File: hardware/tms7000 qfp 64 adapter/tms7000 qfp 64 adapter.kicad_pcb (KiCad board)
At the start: 2 copper layers, 45.1 x 52.1 mm, 4 parts, among them J1 qfp 64, U1 DIP40 male pins

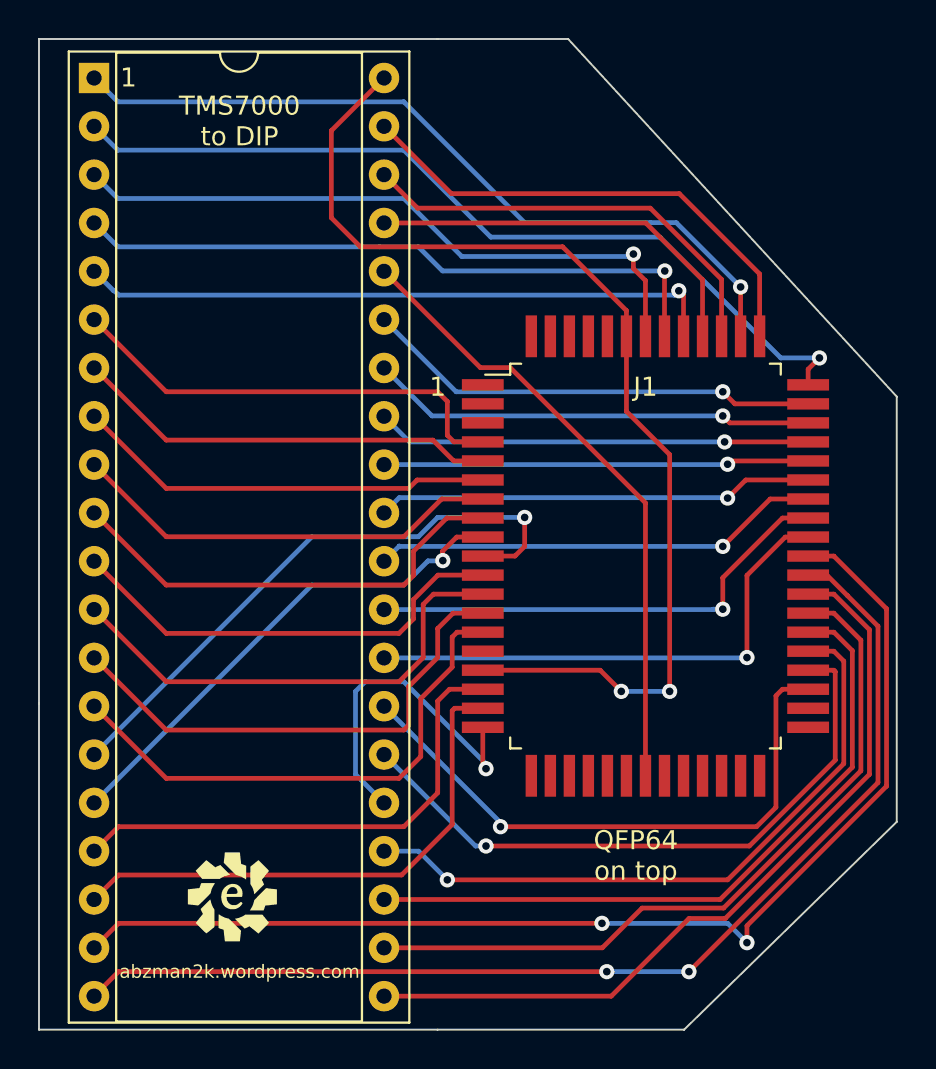
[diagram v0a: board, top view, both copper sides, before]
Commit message: updated qfp64 for fab
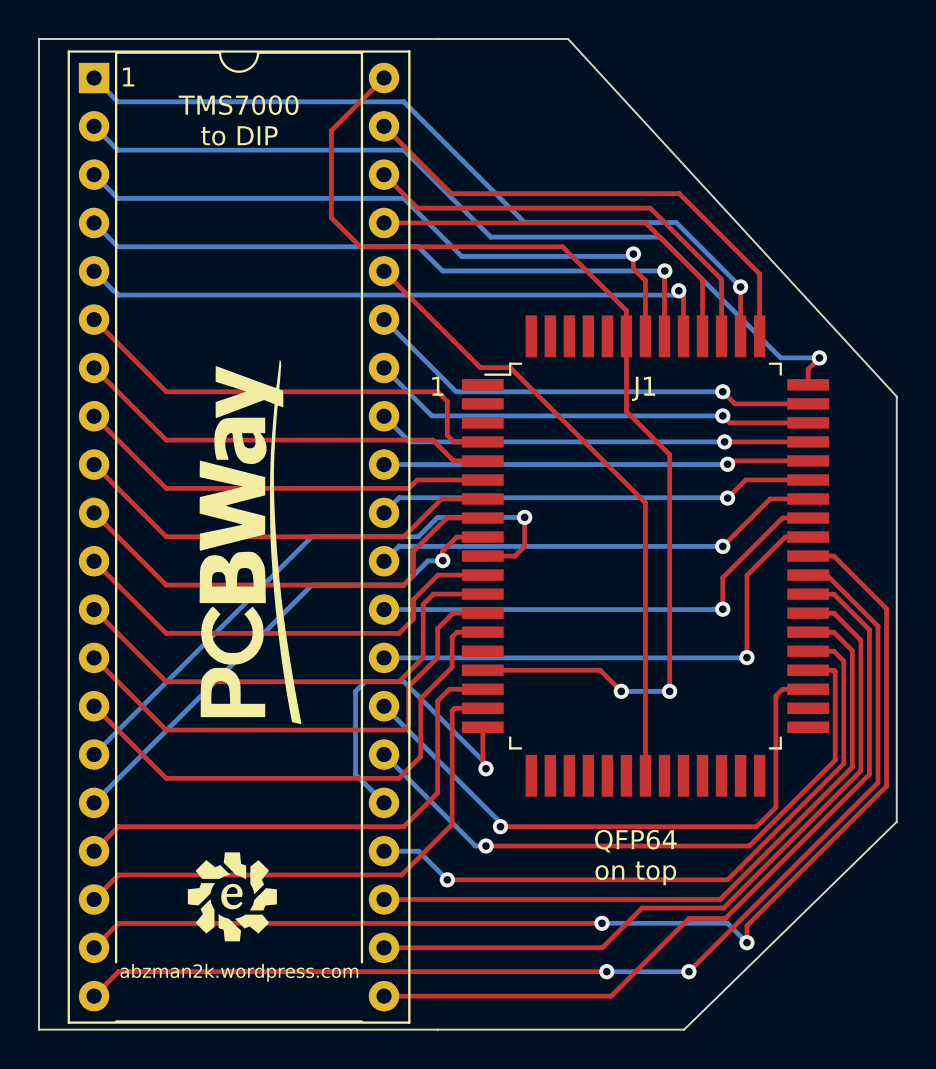
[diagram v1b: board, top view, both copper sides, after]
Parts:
- added G***: LOGO, Evan's parts:pcbway logo, F.Cu at (128.3, 73.0)
